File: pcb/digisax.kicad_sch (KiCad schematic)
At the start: 4 parts, among them SW1 SW_Push, U1 MAX98357A, U2 MPXV7007

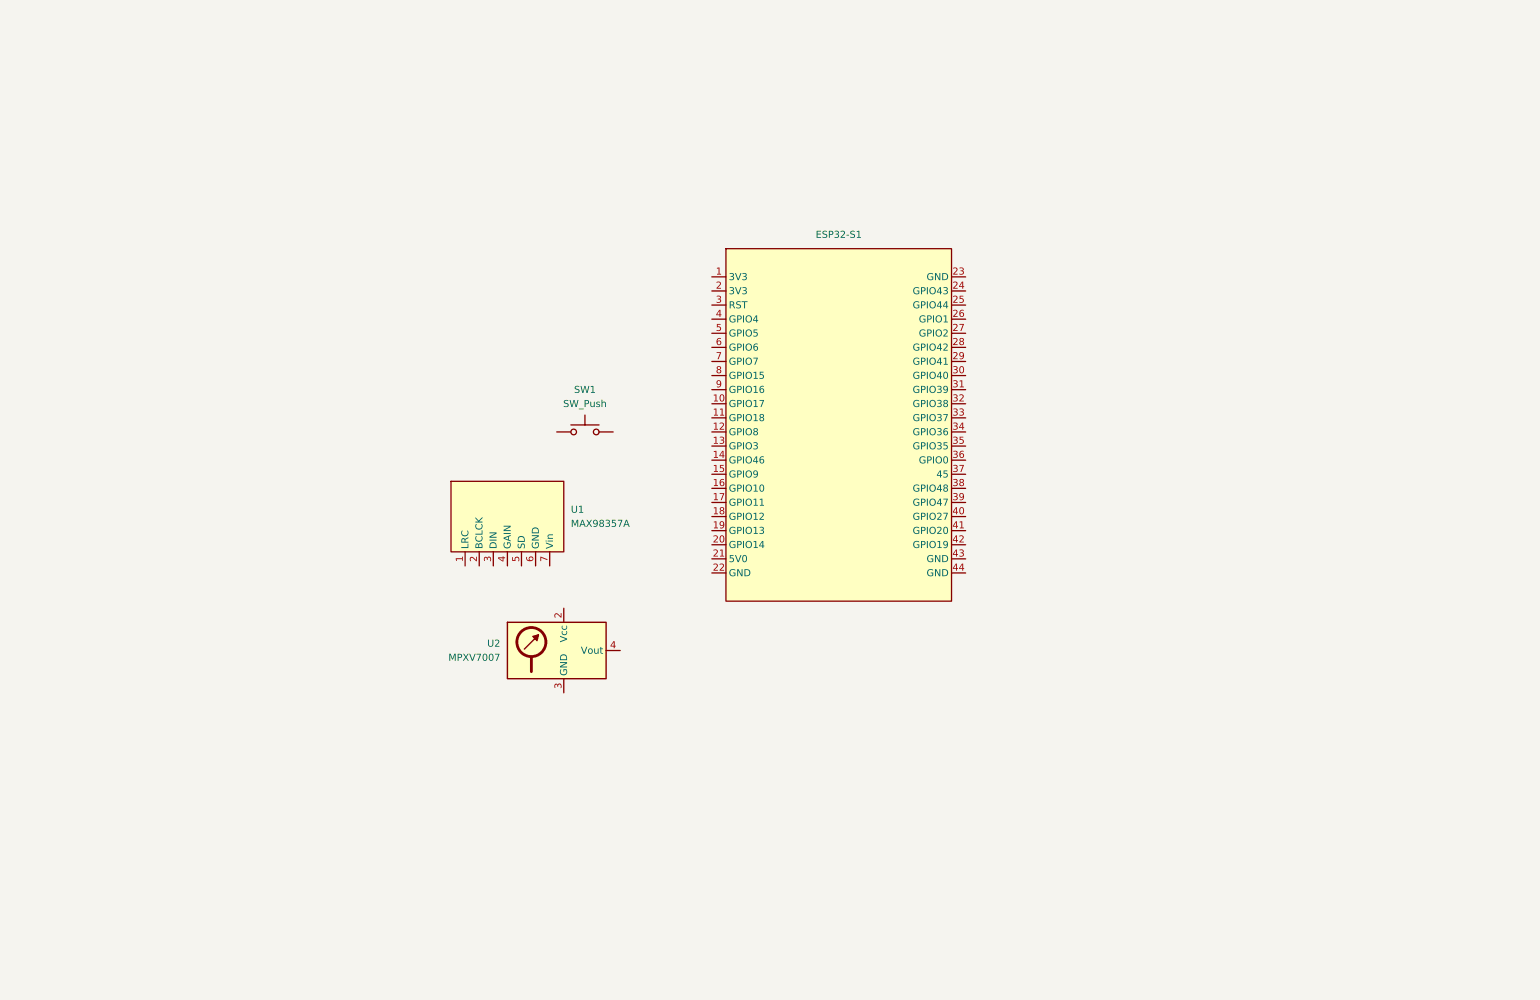
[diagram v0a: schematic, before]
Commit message: started to added switches for keys
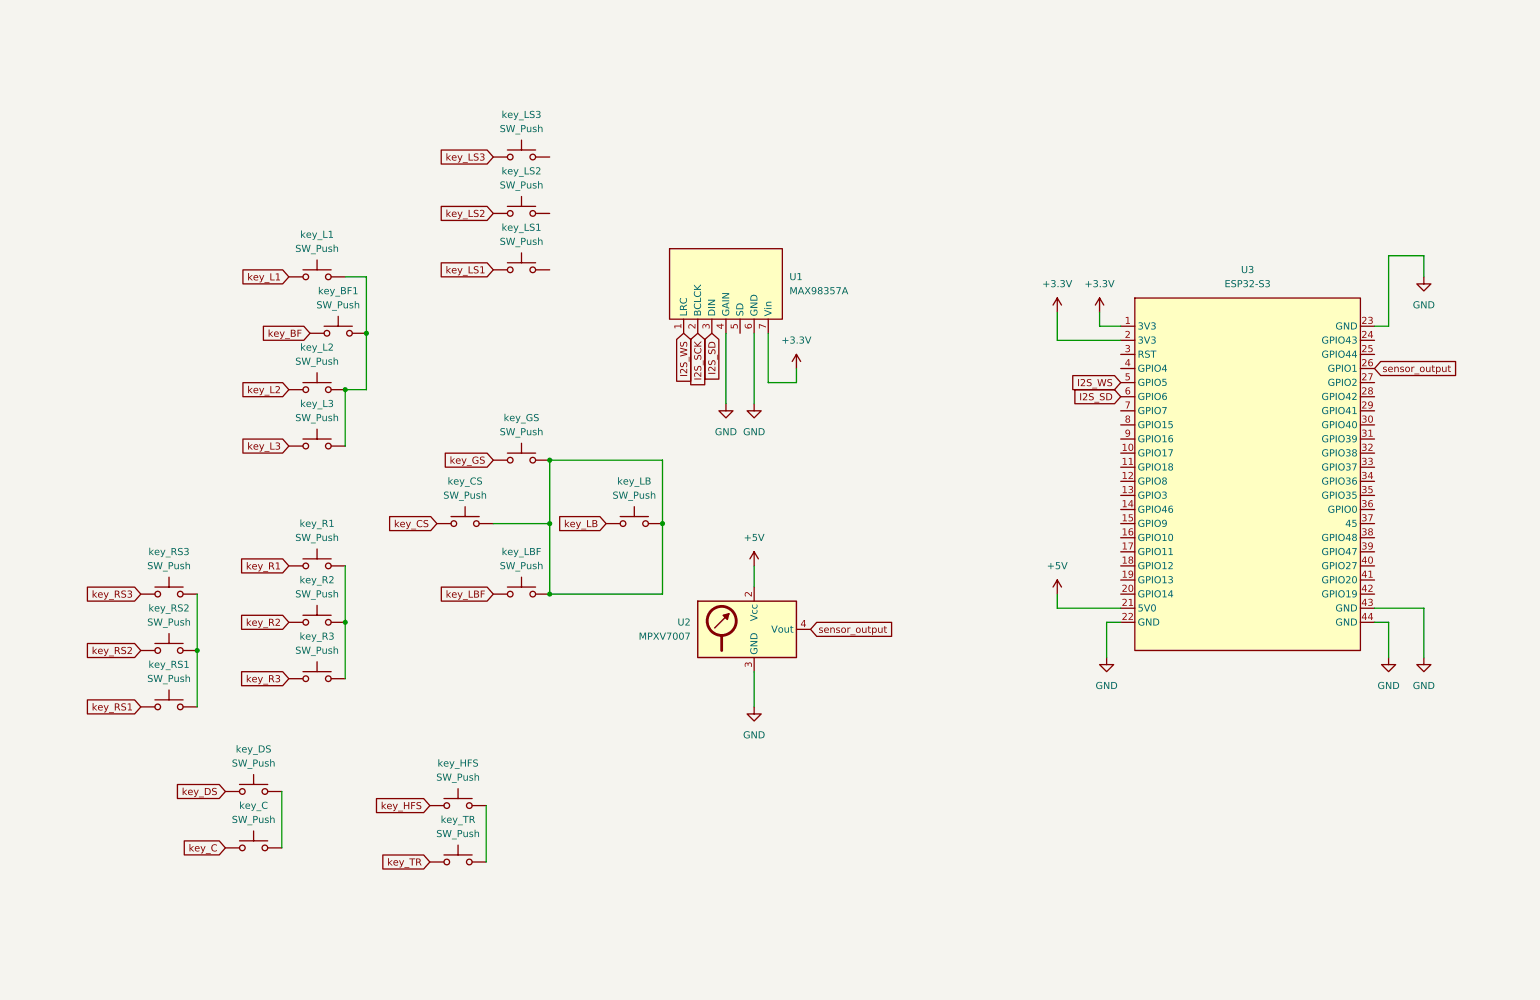
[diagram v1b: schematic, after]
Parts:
- removed ESP32-S1: (no value), symbol 1_ESP32-S3-DevKitC-1:ESP32-S3-DevKitC-1
- added U3: ESP32-S3, symbol 1_ESP32-S3-DevKitC-1:ESP32-S3-DevKitC-1
- added key_BF1, key_C, key_CS, key_DS, key_GS, key_HFS, key_L1, key_L2, key_L3, key_LB, key_LBF, key_LS1, key_LS2, key_LS3, key_R2, key_R3, key_RS1, key_RS2, key_RS3, key_TR: SW_Push, symbol Switch:SW_Push
- renumbered SW1 to key_R1
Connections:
- net +5V: now reaches U2.2 (Vcc)
- net +5V: now also U3.21 (5V0)
- net GND: now reaches U2.3 (GND)
- net GND: now also U1.4 (GAIN), U1.6 (GND), U3.22 (GND), U3.23 (GND), U3.43 (GND), U3.44 (GND)
- net sensor_output: now reaches U2.4 (Vout)
- net sensor_output: now also U3.26 (GPIO1)
- net I2S_WS: now reaches U1.1 (LRC)
- net I2S_WS: now also U3.5 (GPIO5)
- net I2S_SCK: now reaches U1.2 (BCLCK)
- net I2S_SD: now reaches U1.3 (DIN)
- net I2S_SD: now also U3.6 (GPIO6)
- net +3.3V: now reaches U1.7 (Vin)
- net +3.3V: now also U3.1 (3V3), U3.2 (3V3)
- net key_R1: now reaches key_R1.1
- net at key_R1.2: now also key_R2.2, key_R3.2
- new net: key_C.2, key_DS.2
- new net: key_BF1.2, key_L1.2, key_L2.2, key_L3.2
- new net: key_CS.2, key_GS.2, key_LB.2, key_LBF.2
- new net: key_RS1.2, key_RS2.2, key_RS3.2
- new net: key_HFS.2, key_TR.2
- new net key_BF: key_BF1.1
- new net key_C: key_C.1
- new net key_CS: key_CS.1
- new net key_DS: key_DS.1
- new net key_GS: key_GS.1
- new net key_HFS: key_HFS.1
- new net key_L1: key_L1.1
- new net key_L2: key_L2.1
- new net key_L3: key_L3.1
- new net key_LB: key_LB.1
- new net key_LBF: key_LBF.1
- new net key_LS1: key_LS1.1
- new net key_LS2: key_LS2.1
- new net key_LS3: key_LS3.1
- new net key_R2: key_R2.1
- new net key_R3: key_R3.1
- new net key_RS1: key_RS1.1
- new net key_RS2: key_RS2.1
- new net key_RS3: key_RS3.1
- new net key_TR: key_TR.1
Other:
- moved on the sheet: U1, U2, key_R1

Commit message: added all switches, update symbols
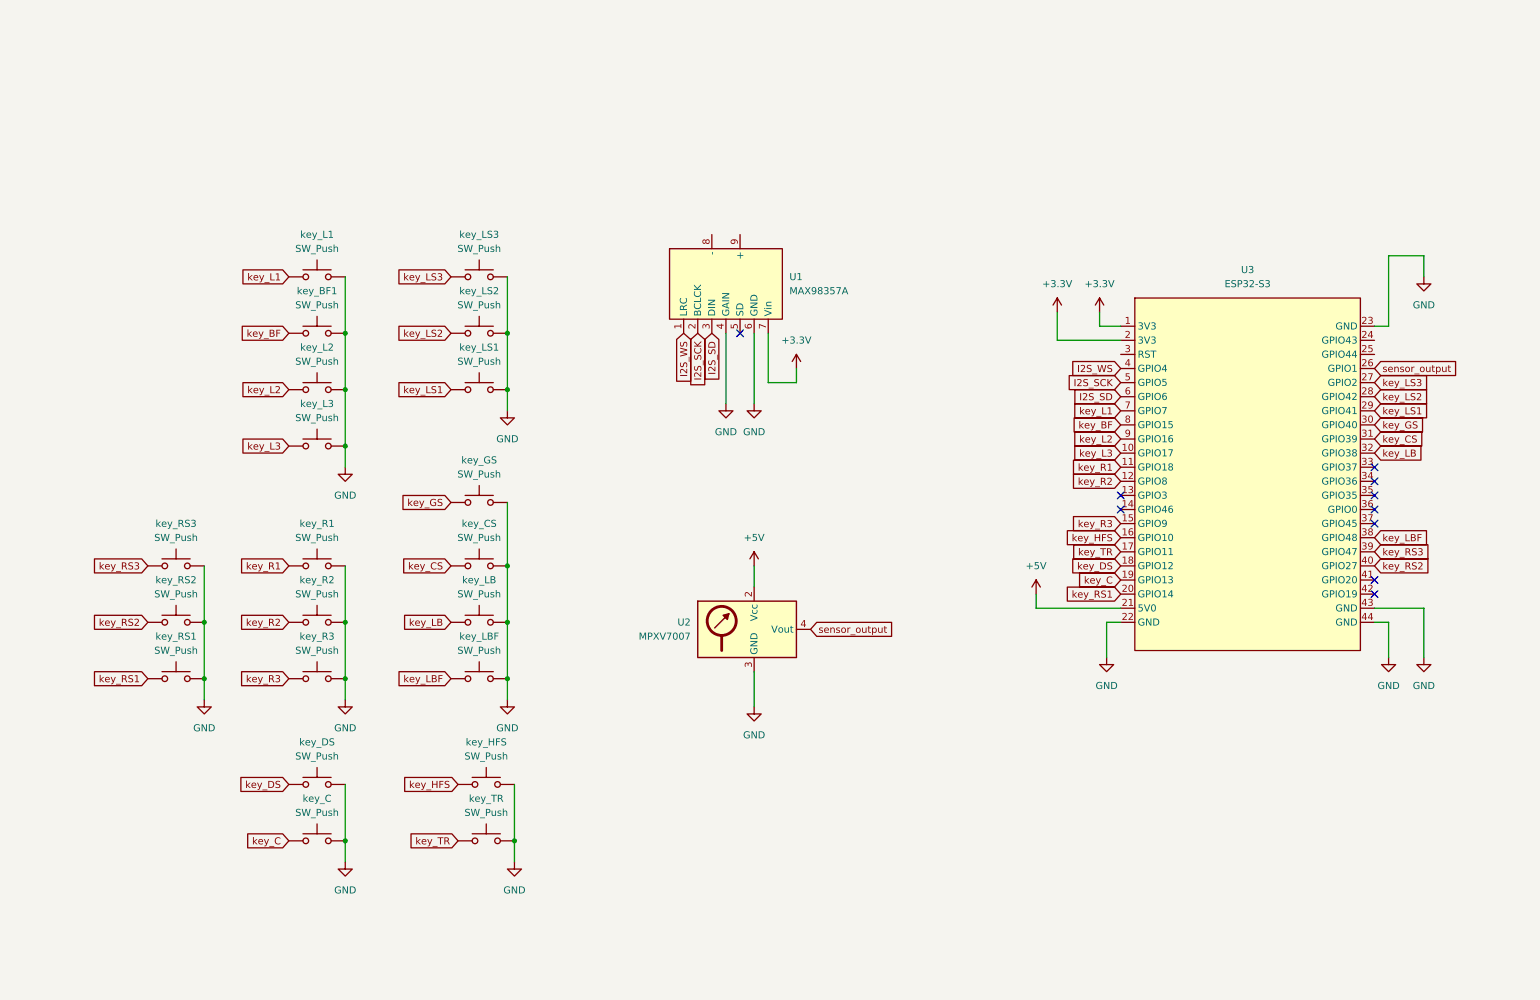
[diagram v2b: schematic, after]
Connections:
- net GND: now also key_BF1.2, key_C.2, key_CS.2, key_DS.2, key_GS.2, key_HFS.2, key_L1.2, key_L2.2, key_L3.2, key_LB.2, key_LBF.2, key_LS1.2, key_LS2.2, key_LS3.2, key_R1.2, key_R2.2, key_R3.2, key_RS1.2, key_RS2.2, key_RS3.2, key_TR.2
- net I2S_SCK: now also U3.5 (GPIO5)
- net I2S_WS: now also U3.4 (GPIO4); no longer U3.5 (GPIO5)
- net key_BF: now also U3.8 (GPIO15)
- net key_C: now also U3.19 (GPIO13)
- net key_CS: now also U3.31 (GPIO39)
- net key_DS: now also U3.18 (GPIO12)
- net key_GS: now also U3.30 (GPIO40)
- net key_HFS: now also U3.16 (GPIO10)
- net key_L1: now also U3.7 (GPIO7)
- net key_L2: now also U3.9 (GPIO16)
- net key_L3: now also U3.10 (GPIO17)
- net key_LB: now also U3.32 (GPIO38)
- net key_LBF: now also U3.38 (GPIO48)
- net key_LS1: now also U3.29 (GPIO41)
- net key_LS2: now also U3.28 (GPIO42)
- net key_LS3: now also U3.27 (GPIO2)
- net key_R1: now also U3.11 (GPIO18)
- net key_R2: now also U3.12 (GPIO8)
- net key_R3: now also U3.15 (GPIO9)
- net key_RS1: now also U3.20 (GPIO14)
- net key_RS2: now also U3.40 (GPIO27)
- net key_RS3: now also U3.39 (GPIO47)
- net key_TR: now also U3.17 (GPIO11)
- no-connect marks 0 -> 10
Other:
- moved on the sheet: key_BF1, key_C, key_CS, key_DS, key_GS, key_HFS, key_LB, key_LBF, key_LS1, key_LS2, key_LS3, key_RS1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

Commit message: added adc to schematic
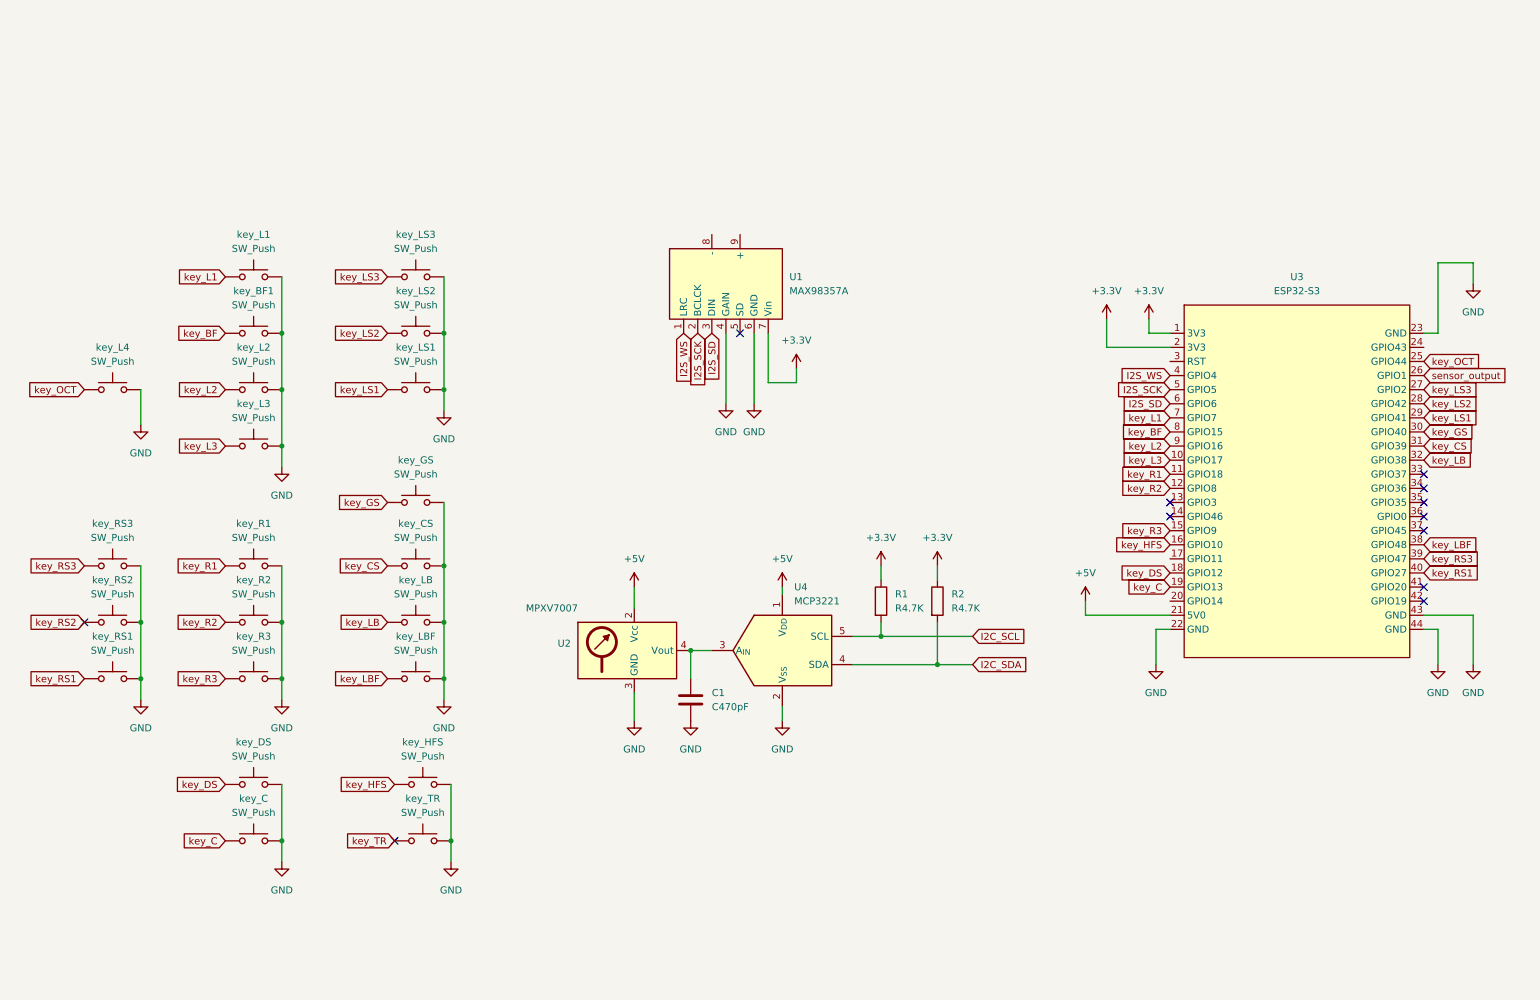
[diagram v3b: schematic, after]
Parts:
- added C1: C470pF, symbol Device:C
- added R1, R2: R4.7K, symbol Device:R
- added U4: MCP3221, Package_TO_SOT_SMD:SOT-23-5, symbol Analog_ADC:MCP3221
- added key_L4: SW_Push, symbol Switch:SW_Push
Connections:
- net +3.3V: now also R1.1, R2.1
- net +5V: now also U4.1 (V_{DD})
- net GND: now also C1.2, U4.2 (V_{SS}), key_L4.2
- net key_RS1: now also U3.40 (GPIO27); no longer U3.20 (GPIO14)
- net key_RS2: no longer U3.40 (GPIO27)
- net key_TR: no longer U3.17 (GPIO11)
- net sensor_output: no longer U2.4 (Vout)
- net key_OCT: now reaches U3.25 (GPIO44)
- net key_OCT: now also key_L4.1
- new net: C1.1, U2.4 (Vout), U4.3 (A_{IN})
- new net I2C_SCL: R1.2, U4.5 (SCL)
- new net I2C_SDA: R2.2, U4.4 (SDA)
- no-connect marks 10 -> 12
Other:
- moved on the sheet: U2, U3, key_BF1, key_C, key_CS, key_DS, key_GS, key_HFS, key_L1, key_L2, key_L3, key_LB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

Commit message: added new dac to schem
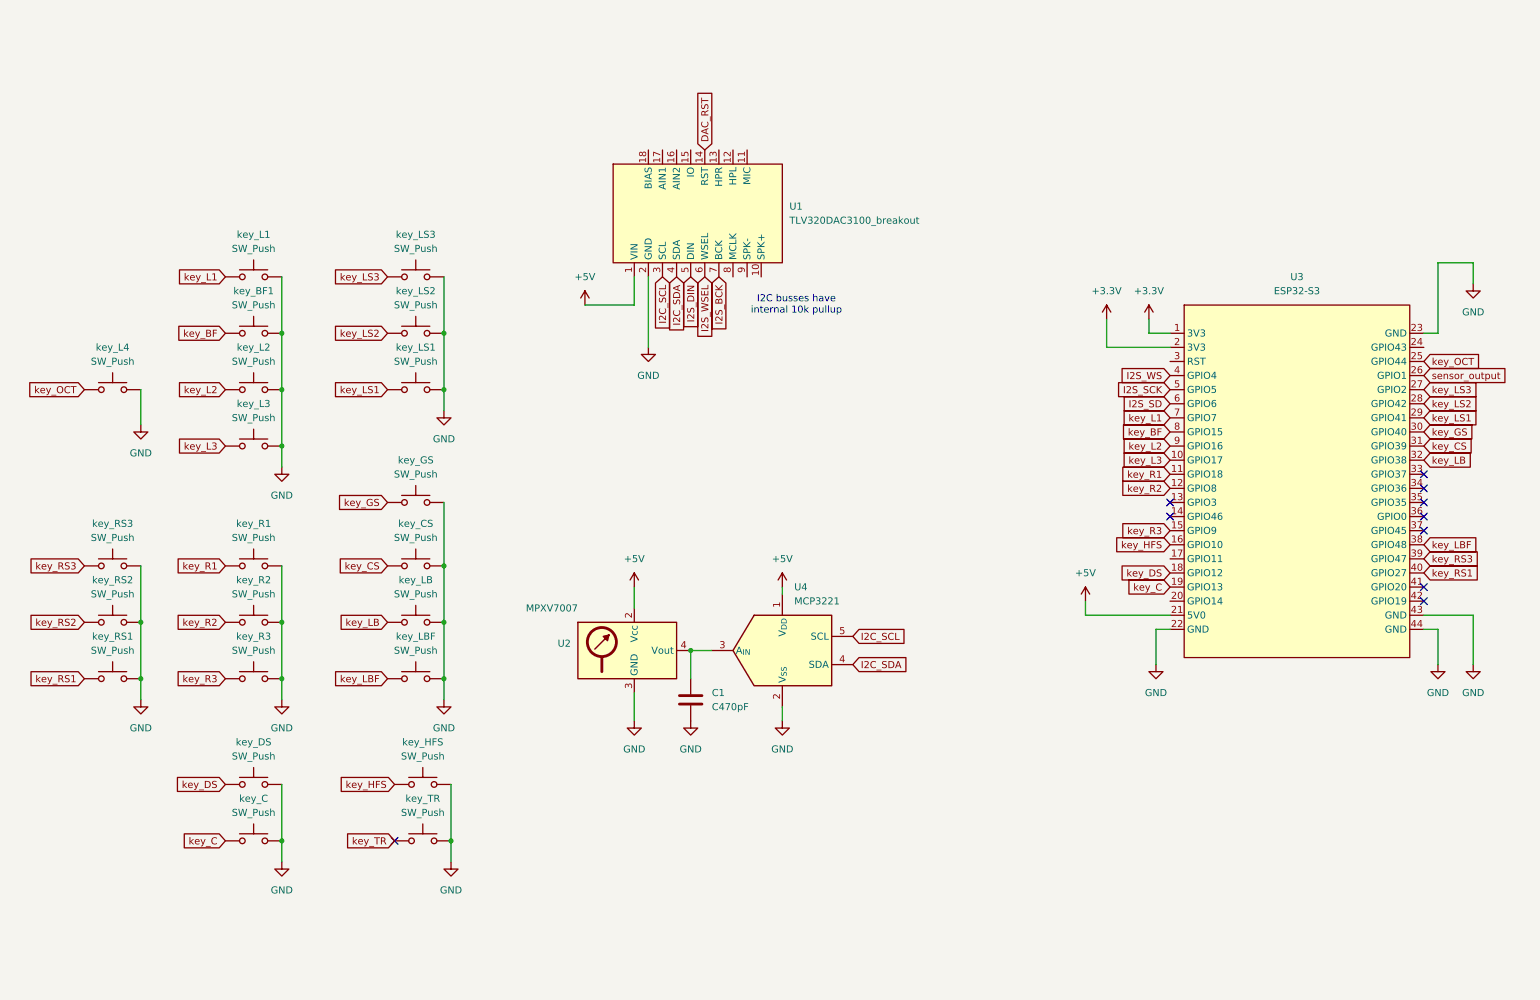
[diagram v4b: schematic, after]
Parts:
- removed R1, R2: R4.7K, symbol Device:R
- removed U1: MAX98357A, symbol Audio:MAX98357A_breakout
- added U1: TLV320DAC3100_breakout, symbol Audio:TLV320DAC3100_breakout
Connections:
- net +5V: now also U1.1 (VIN)
- net GND: now also U1.2 (GND)
- net I2C_SCL: now also U1.3 (SCL)
- net I2C_SDA: now also U1.4 (SDA)
- new net DAC_RST: U1.14 (RST)
- new net I2S_BCK: U1.7 (BCK)
- new net I2S_DIN: U1.5 (DIN)
- new net I2S_WSEL: U1.6 (WSEL)
- no-connect marks 12 -> 10
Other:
- note added: "I2C busses have internal 10k pullup"

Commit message: started matrix wiring
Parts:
- added D1: 1N4148, Diode_THT:D_DO-35_SOD27_P7.62mm_Horizontal, symbol Diode:1N4148
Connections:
- net GND: no longer key_BF1.2, key_C.2, key_CS.2, key_DS.2, key_GS.2, key_HFS.2, key_L1.2, key_L2.2, key_L3.2, key_L4.2, key_LB.2, key_LBF.2, key_LS1.2, key_LS2.2, key_LS3.2, key_R1.2, key_R2.2, key_R3.2, key_RS1.2, key_RS2.2, key_RS3.2, key_TR.2
- net key_BF: no longer U3.8 (GPIO15)
- net key_C: no longer U3.19 (GPIO13)
- net key_CS: no longer U3.31 (GPIO39)
- net key_DS: no longer U3.18 (GPIO12)
- net key_GS: no longer U3.30 (GPIO40)
- net key_HFS: no longer U3.16 (GPIO10)
- net key_L1: no longer U3.7 (GPIO7)
- net key_L2: no longer U3.9 (GPIO16)
- net key_L3: no longer U3.10 (GPIO17)
- net key_LB: no longer U3.32 (GPIO38)
- net key_LBF: no longer U3.38 (GPIO48)
- net key_LS1: no longer U3.29 (GPIO41)
- net key_LS2: no longer U3.28 (GPIO42)
- net key_LS3: no longer U3.27 (GPIO2)
- net key_R1: no longer U3.11 (GPIO18)
- net key_R2: no longer U3.12 (GPIO8)
- net key_R3: no longer U3.15 (GPIO9)
- net key_RS1: no longer U3.40 (GPIO27)
- net key_RS3: no longer U3.39 (GPIO47)
- new net: key_BF1.2, key_L1.2, key_L2.2, key_L3.2, key_R1.2, key_R2.2, key_R3.2
- new net: key_LS1.2, key_LS2.2, key_LS3.2
- new net: key_C.2, key_DS.2
- new net: key_CS.2, key_GS.2, key_LB.2, key_LBF.2
- new net: key_RS1.2, key_RS2.2, key_RS3.2
- new net: key_HFS.2, key_TR.2
- no-connect marks 10 -> 9
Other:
- moved on the sheet: C1, U1, U2, U4, key_C, key_CS, key_DS, key_GS, key_HFS, key_L4, key_LB, key_LBF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
